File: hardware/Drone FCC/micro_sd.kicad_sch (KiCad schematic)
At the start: 7 parts, among them J21 Micro_SD_Card_Det_Hirose_DM3AT

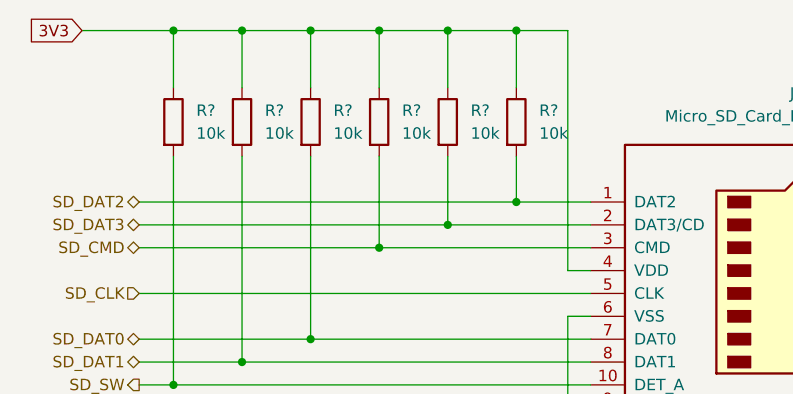
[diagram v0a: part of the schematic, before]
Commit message: changed usb 2.0 AB connector for usb 2.0 B
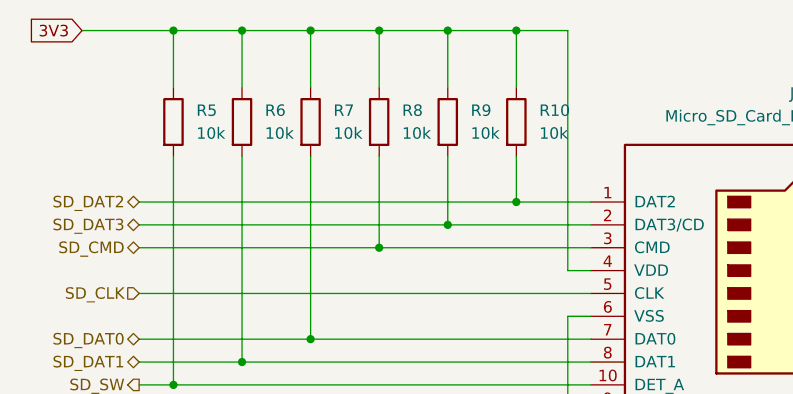
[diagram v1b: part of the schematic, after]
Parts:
- gave numbers to parts that had none: 6
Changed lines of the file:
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@@
   (symbol (lib_id "Device:R") (at 76.2 53.975 0) (unit 1)
     (in_bom yes) (on_board yes) (fields_autoplaced)
-    (property "Reference" "R?" (id 0) (at 78.74 52.7049 0)
+    (property "Reference" "R6" (id 0) (at 78.74 52.7049 0)
       (effects (font (size 1.27 1.27)) (justify left))
     )
@@
   (symbol (lib_id "Device:R") (at 83.82 53.975 0) (unit 1)
     (in_bom yes) (on_board yes) (fields_autoplaced)
-    (property "Reference" "R?" (id 0) (at 86.36 52.7049 0)
+    (property "Reference" "R7" (id 0) (at 86.36 52.7049 0)
       (effects (font (size 1.27 1.27)) (justify left))
     )
@@
   (symbol (lib_id "Device:R") (at 99.06 53.975 0) (unit 1)
     (in_bom yes) (on_board yes) (fields_autoplaced)
-    (property "Reference" "R?" (id 0) (at 101.6 52.7049 0)
+    (property "Reference" "R9" (id 0) (at 101.6 52.7049 0)
       (effects (font (size 1.27 1.27)) (justify left))
     )
@@
   (symbol (lib_id "Device:R") (at 68.58 53.975 0) (unit 1)
     (in_bom yes) (on_board yes) (fields_autoplaced)
-    (property "Reference" "R?" (id 0) (at 71.12 52.7049 0)
+    (property "Reference" "R5" (id 0) (at 71.12 52.7049 0)
       (effects (font (size 1.27 1.27)) (justify left))
     )
@@
   (symbol (lib_id "Device:R") (at 106.68 53.975 0) (unit 1)
     (in_bom yes) (on_board yes) (fields_autoplaced)
-    (property "Reference" "R?" (id 0) (at 109.22 52.7049 0)
+    (property "Reference" "R10" (id 0) (at 109.22 52.7049 0)
       (effects (font (size 1.27 1.27)) (justify left))
     )
@@
   (symbol (lib_id "Device:R") (at 91.44 53.975 0) (unit 1)
     (in_bom yes) (on_board yes) (fields_autoplaced)
-    (property "Reference" "R?" (id 0) (at 93.98 52.7049 0)
+    (property "Reference" "R8" (id 0) (at 93.98 52.7049 0)
       (effects (font (size 1.27 1.27)) (justify left))
     )
@@
   (symbol (lib_id "power:GND") (at 112.395 95.885 0) (unit 1)
     (in_bom yes) (on_board yes) (fields_autoplaced)
-    (property "Reference" "#PWR?" (id 0) (at 112.395 102.235 0)
+    (property "Reference" "#PWR0117" (id 0) (at 112.395 102.235 0)
       (effects (font (size 1.27 1.27)) hide)
     )

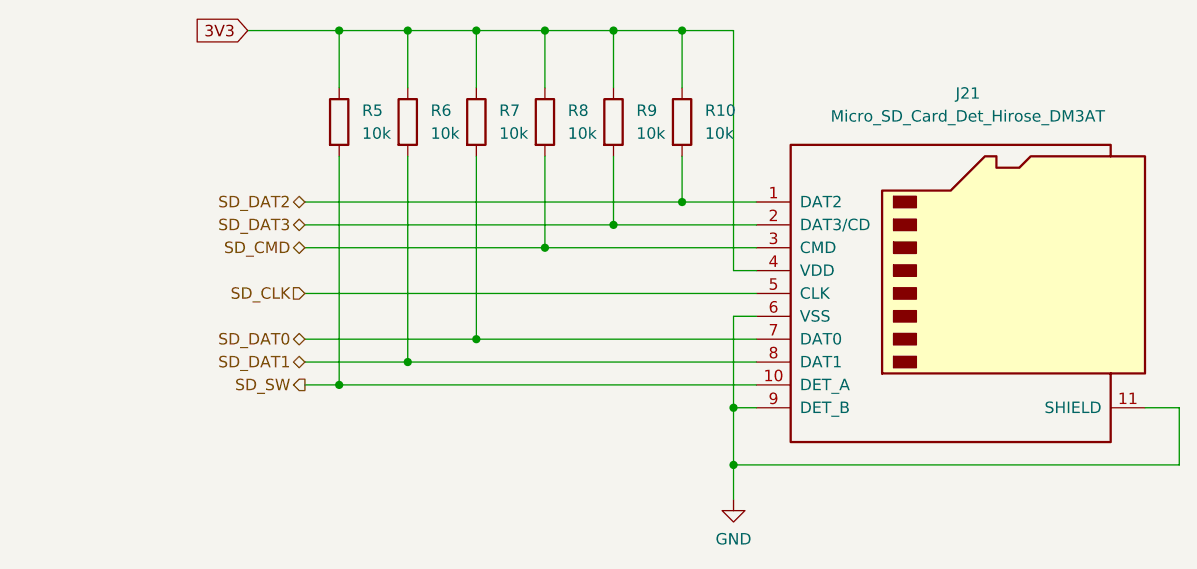
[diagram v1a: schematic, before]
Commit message: rearranged FCC schematic
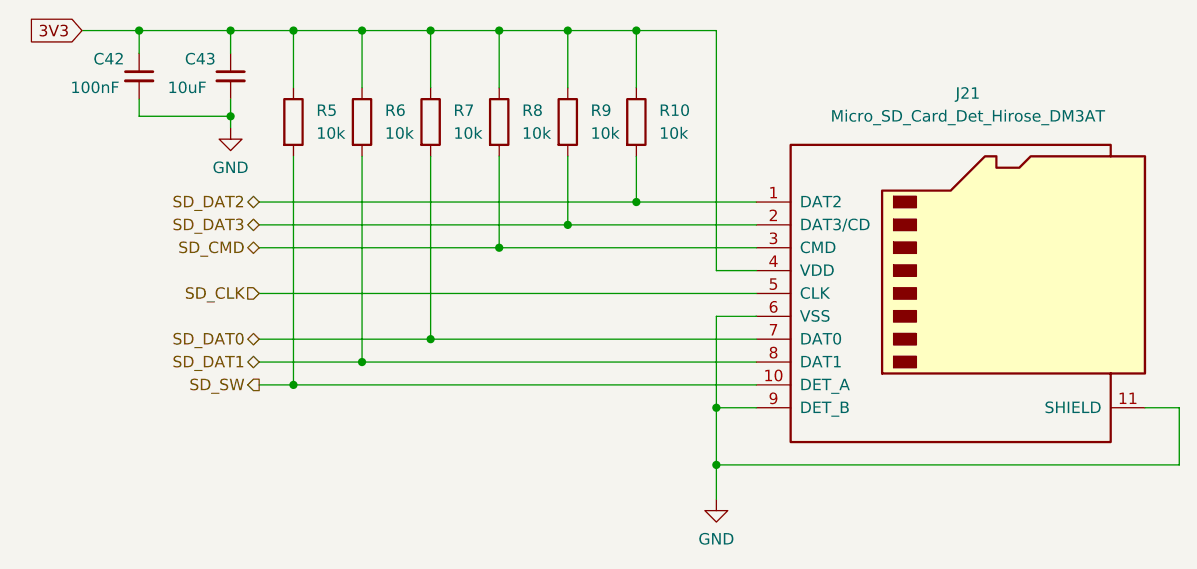
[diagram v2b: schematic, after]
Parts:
- added C42: 100nF, symbol Device:C_Small
- added C43: 10uF, symbol Device:C_Small
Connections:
- net 3V3: now also C42.1, C43.1
- net GND: now also C42.2, C43.2
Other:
- moved on the sheet: R10, R5, R6, R7, R8, R9

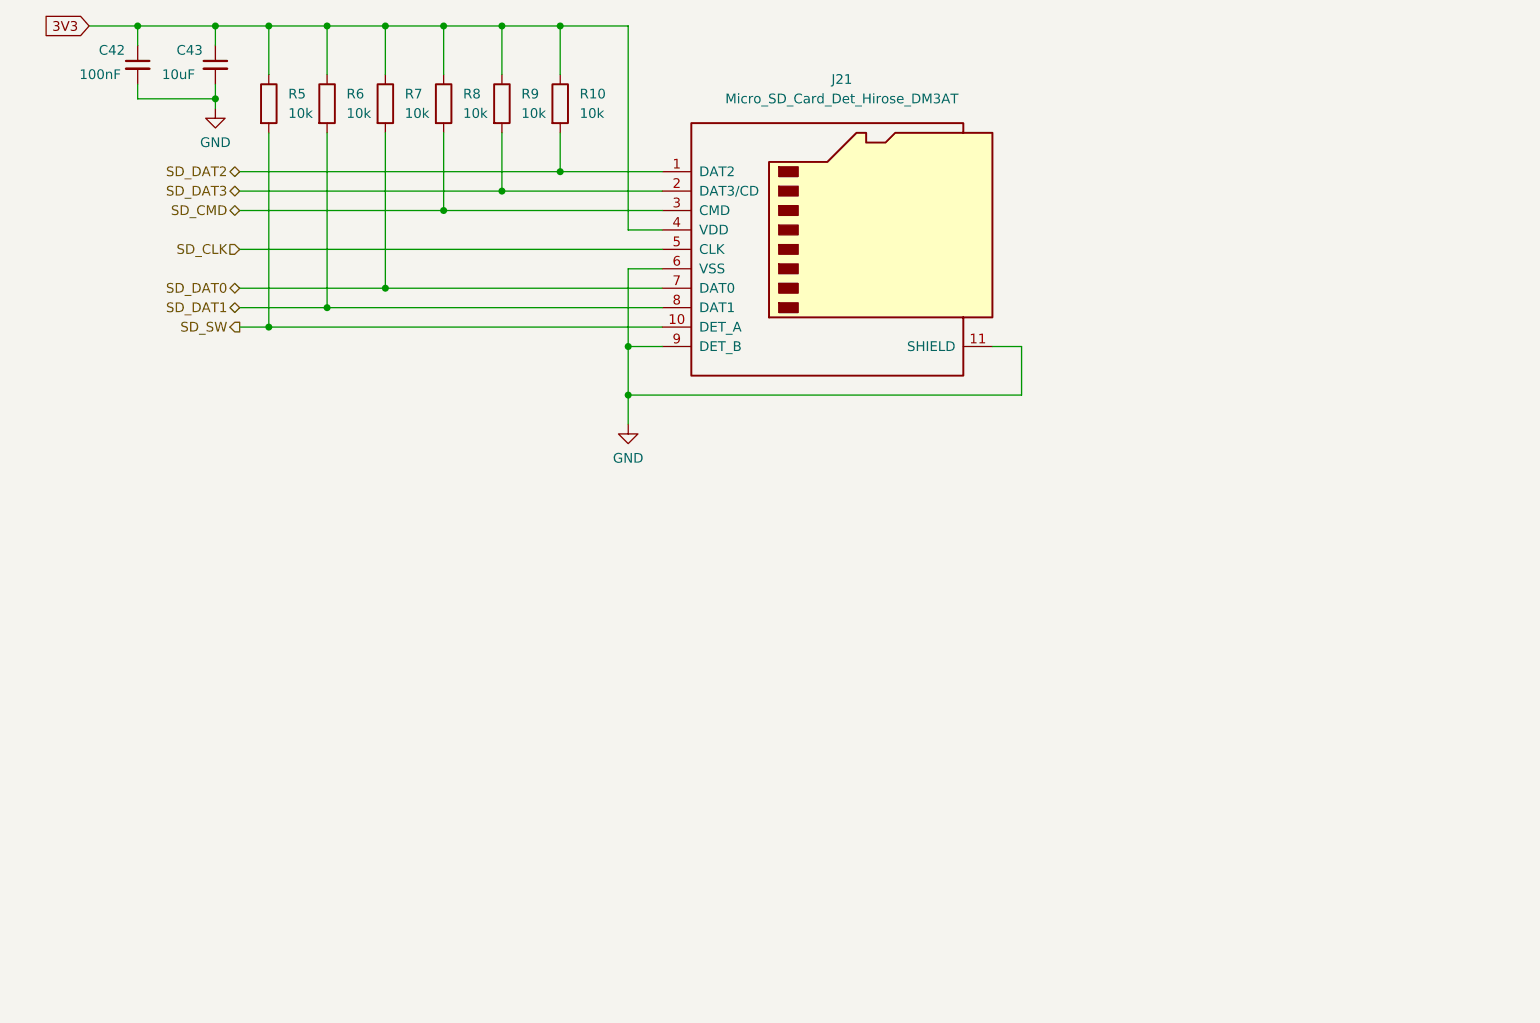
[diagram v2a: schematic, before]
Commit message: add external communication connectors
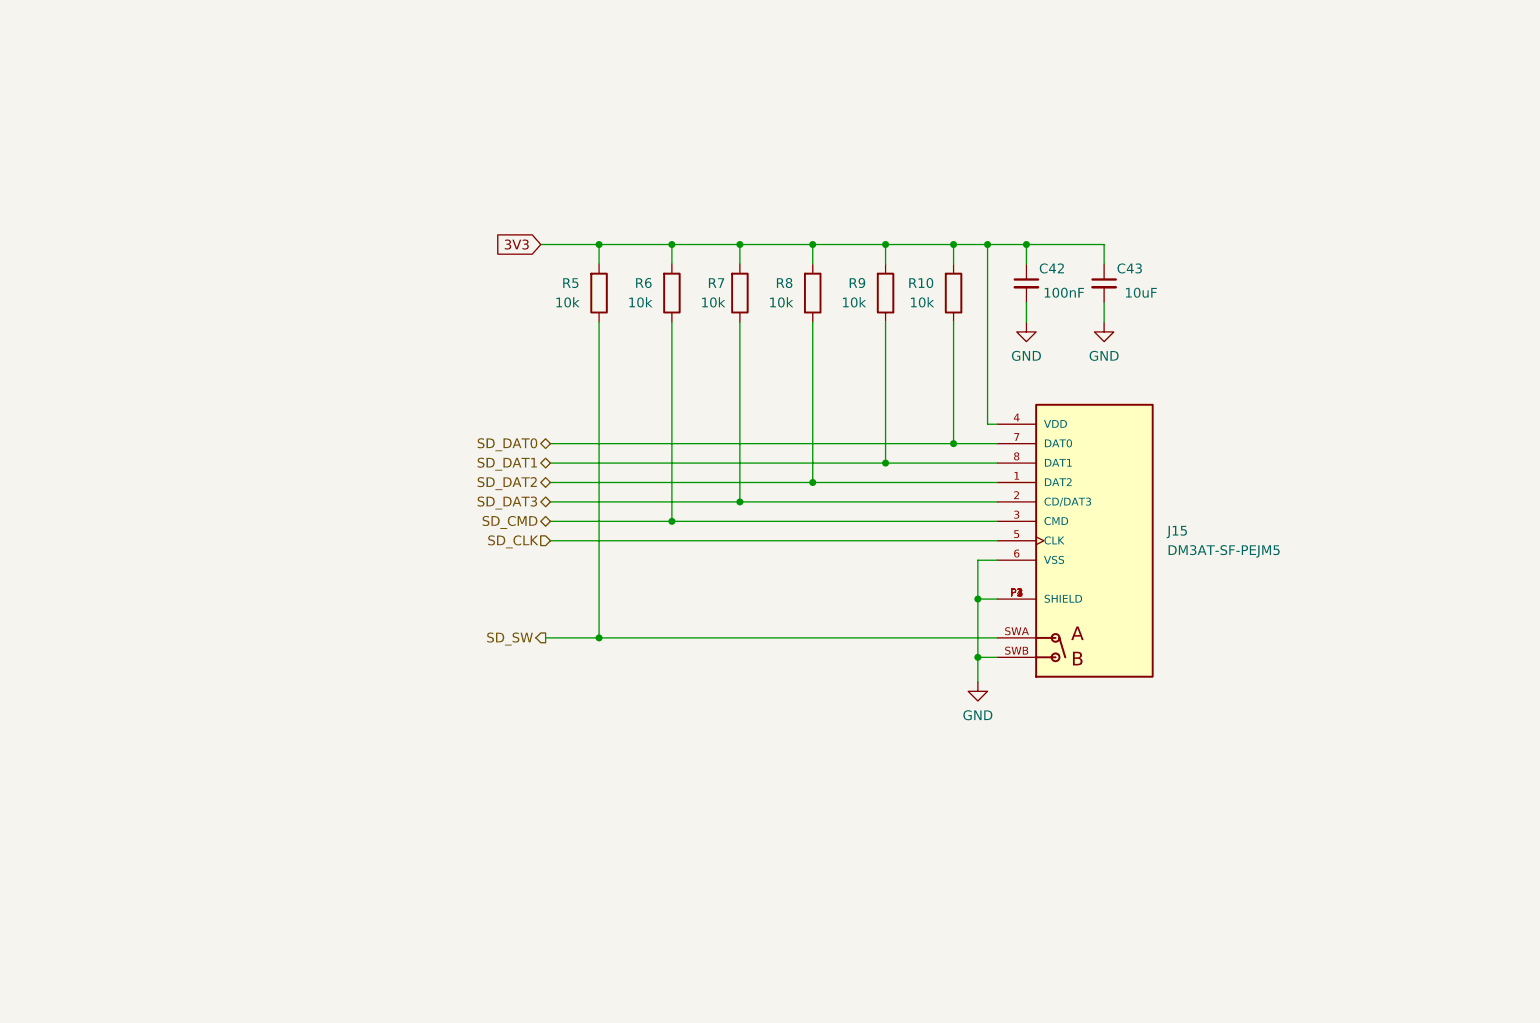
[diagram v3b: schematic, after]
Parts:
- removed J21: Micro_SD_Card_Det_Hirose_DM3AT, DM3AT-SF-PEJM5:HRS_DM3AT-SF-PEJM5, symbol Connector:Micro_SD_Card_Det_Hirose_DM3AT
- added J15: DM3AT-SF-PEJM5, DM3AT-SF-PEJM5:HRS_DM3AT-SF-PEJM5, symbol DM3AT-SF-PEJM5:DM3AT-SF-PEJM5
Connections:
- net 3V3: now also R10.2, R5.2, R6.2, R7.2, R8.2, R9.2, J15.4 (VDD); no longer R10.1, R5.1, R6.1, R7.1, R8.1, R9.1
- net GND: now also J15.6 (VSS), J15.P1 (SHIELD), J15.P2 (SHIELD), J15.P3 (SHIELD), J15.P4 (SHIELD), J15.SWB
- net SD_CLK: now also J15.5 (CLK)
- net SD_CMD: now also R6.1, J15.3 (CMD); no longer R8.2
- net SD_DAT0: now also R10.1, J15.7 (DAT0); no longer R7.2
- net SD_DAT1: now also R9.1, J15.8 (DAT1); no longer R6.2
- net SD_DAT2: now also R8.1, J15.1 (DAT2); no longer R10.2
- net SD_DAT3: now also R7.1, J15.2 (CD/DAT3); no longer R9.2
- net SD_SW: now also R5.1, J15.SWA; no longer R5.2
